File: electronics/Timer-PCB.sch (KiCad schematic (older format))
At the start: 0 parts

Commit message: init first version of PCB
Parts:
- added C1: 120n, Capacitor_THT_k:C_Axial_L5.1mm_D3.1mm_P7.50mm_Horizontal_k, symbol Device_k:C
- added C2: 2200uF, Capacitor_THT_k:CP_Radial_D13.0mm_P5.00mm_k, symbol Device_k:CP
- added C3: 220uF, Capacitor_THT_k:CP_Radial_D8.0mm_P3.50mm_k, symbol Device_k:CP
- added D1: D_Bridge_+-AA, Diode_THT_k:Diode_Bridge_Round_D8.9mm_k, symbol Device_k:D_Bridge_+-AA
- added D2: LED, LED_THT_k:LED_D5.0mm_Clear_k, symbol Device_k:LED
- added J1: Screw_Terminal_01x02, TerminalBlock_Phoenix_k:TerminalBlock_Phoenix_PT-1,5-2-3.5-H_1x02_P3.50mm_Horizontal_k, symbol Connector_k:Screw_Terminal_01x02
- added J2: Screw_Terminal_01x03, TerminalBlock_Phoenix_k:TerminalBlock_Phoenix_PT-1,5-3-3.5-H_1x03_P3.50mm_Horizontal_k, symbol Connector_k:Screw_Terminal_01x03
- added R1: R120, Resistor_THT_k:R_Axial_DIN0207_L6.3mm_D2.5mm_P10.16mm_Horizontal_k, symbol Device_k:R
- added R2: 2k2, Resistor_THT_k:R_Axial_DIN0207_L6.3mm_D2.5mm_P10.16mm_Horizontal_k, symbol Device_k:R
- added SW1: Rotary_Encoder_Switch, Rotary_Encoder_k:RotaryEncoder_Alps_EC11E-Switch_Vertical_H20mm_CircularMountingHoles_k, symbol Device_k:Rotary_Encoder_Switch
- added U1: L7805, Package_TO_SOT_THT_k:TO-220-3_Horizontal_TabDown_k, symbol Regulator_Linear_k:L7805
- added U2: Teensy-LC, Teensy.pretty:Teensy30_31_32_LC, symbol teensy_library:Teensy-LC
- added U3: 7-Seg_8dig_MAX7219, Display_7Segment_k:7seg_8dig_MAX7219_module, symbol Display_Character_k:7-Seg_8dig_MAX7219
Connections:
- net labels added: +5V, CLK, CS, DIN, GND, SSR, VD
- wire segments 0 -> 54
- no-connect marks 0 -> 33
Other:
- note added: "Power Supply"
- note added: "SolidState Relais output"
- note added: "teensy"

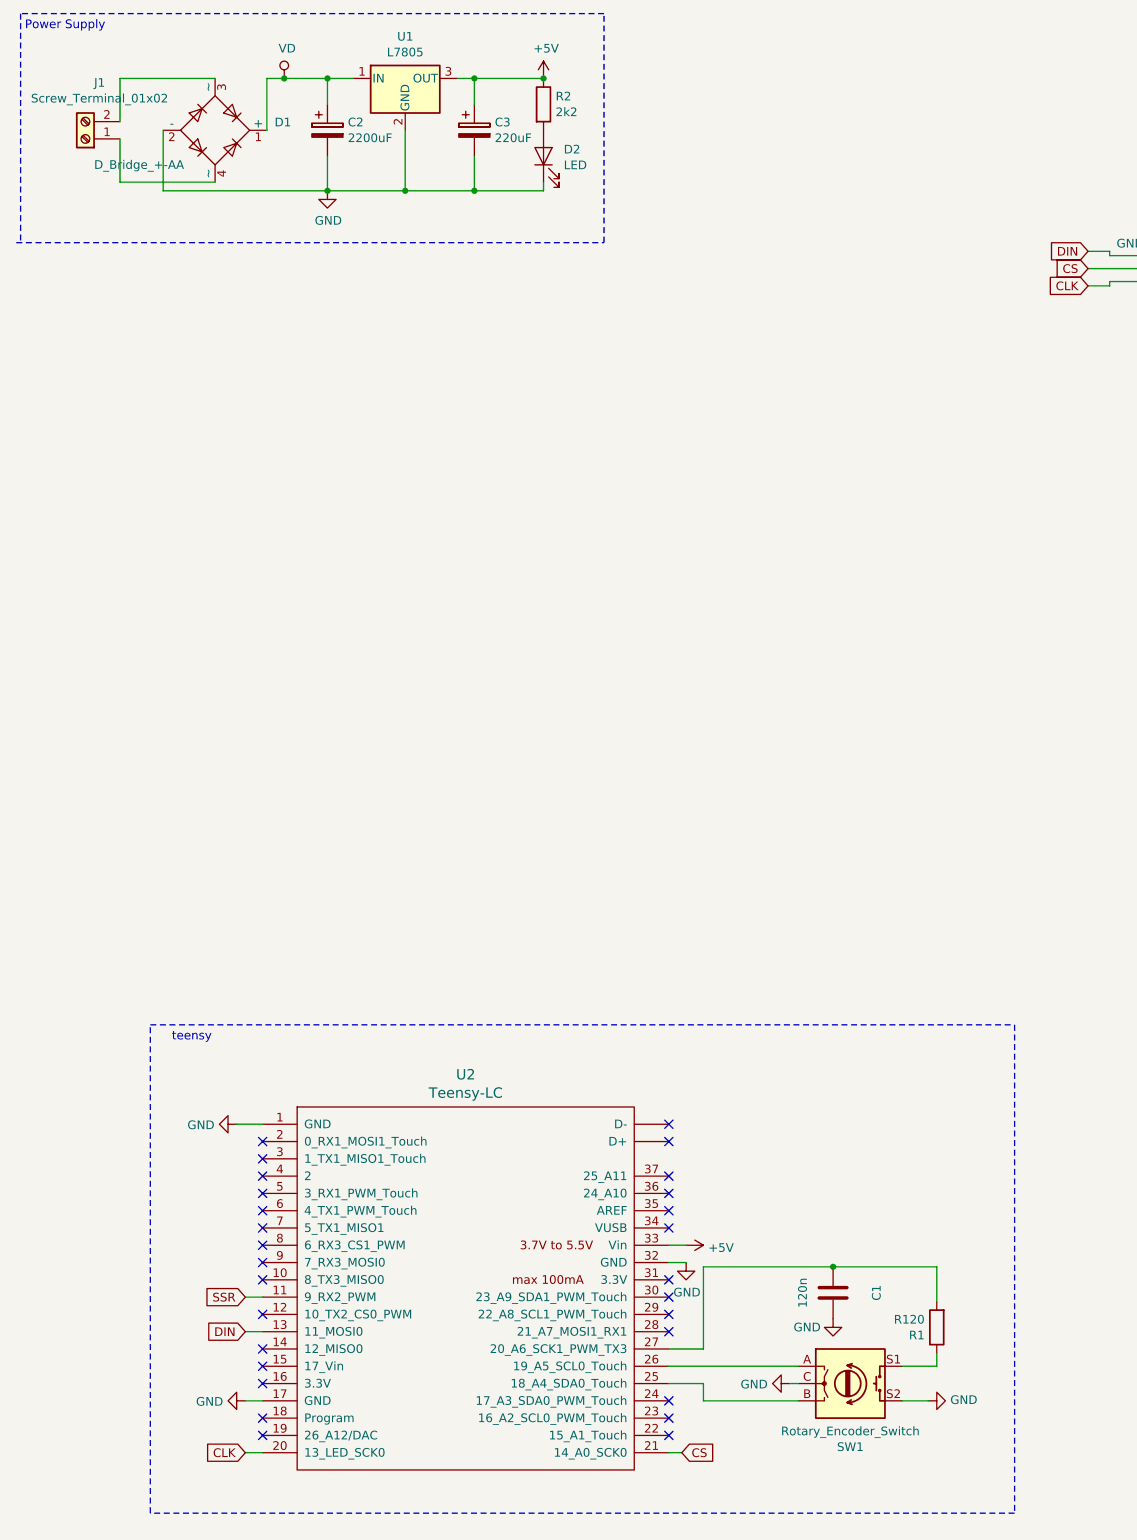
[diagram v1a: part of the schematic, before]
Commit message: changed schematic to use teensy pin for indicator LED (see #3)
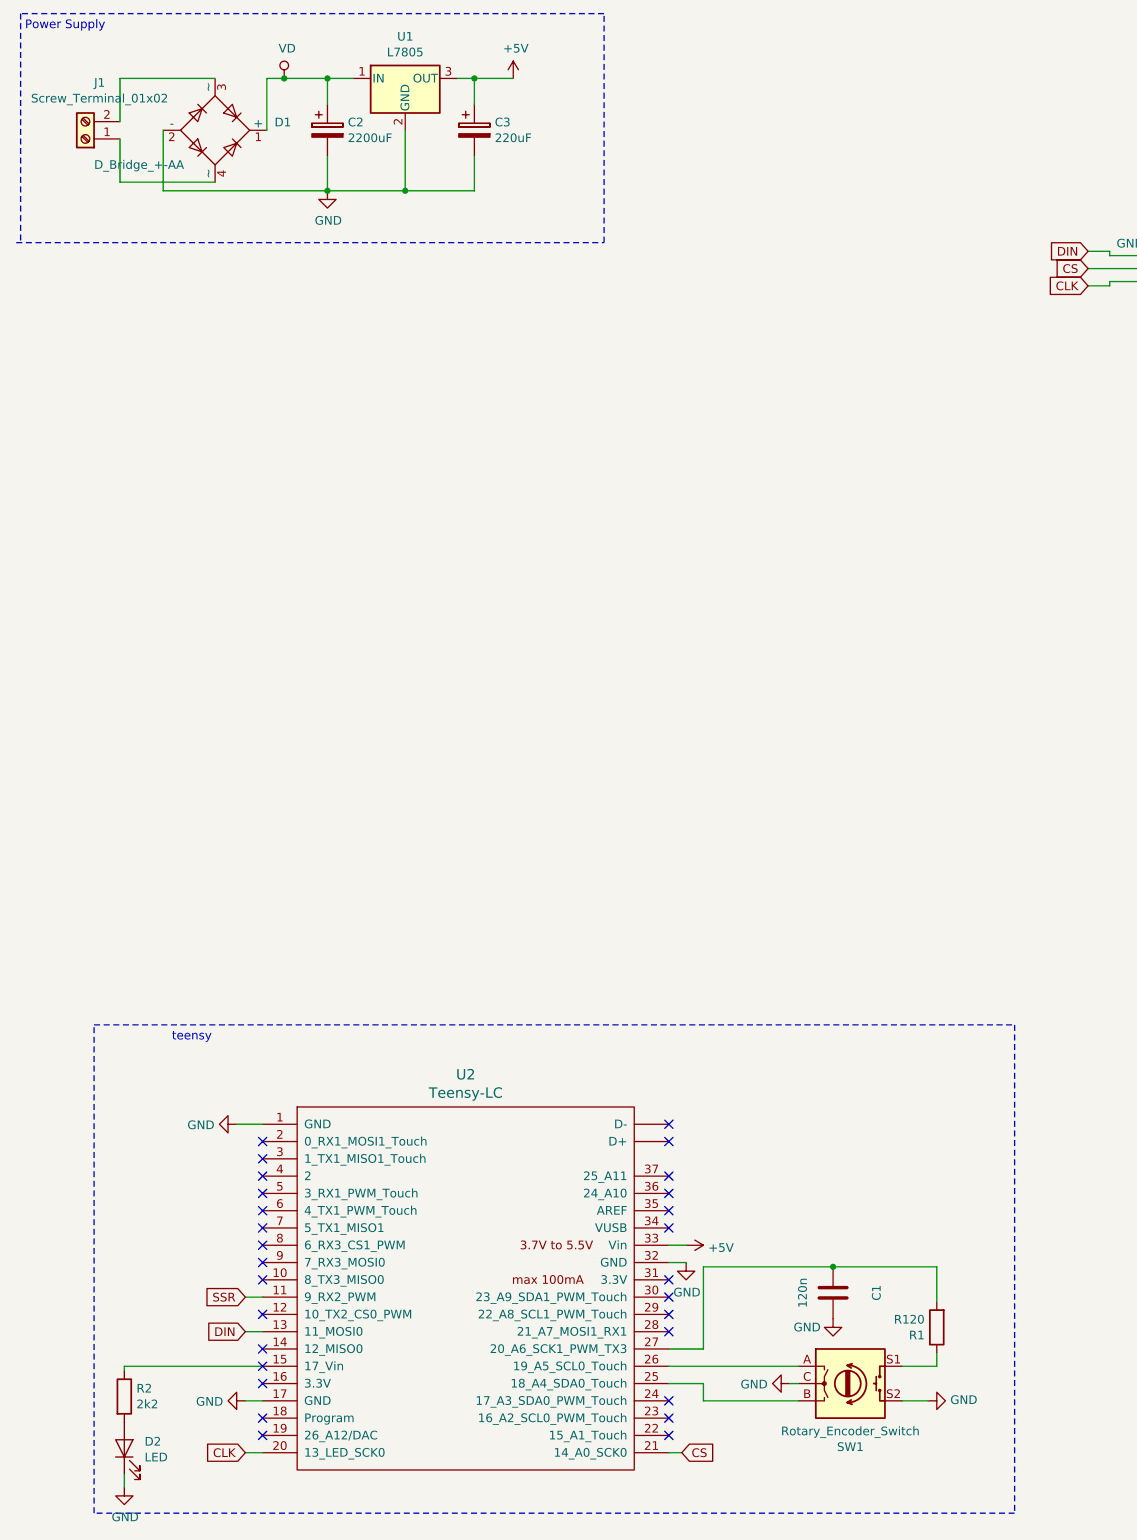
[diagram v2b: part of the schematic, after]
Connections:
- wire segments 54 -> 55
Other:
- moved on the sheet: D2, R2
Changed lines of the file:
@@
 L power_k:+5V #PWR06
 U 1 1 5F7D4ECC
-P 3975 1400
-F 0 "#PWR06" H 3975 1250 50  0001 C CNN
-F 1 "+5V" H 3990 1573 50  0000 C CNN
-F 2 "" H 3975 1400 50  0001 C CNN
-F 3 "" H 3975 1400 50  0001 C CNN
-	1    3975 1400
-	1    0    0    -1
-$EndComp
-Connection ~ 3575 1400
+P 3800 1400
+F 0 "#PWR06" H 3800 1250 50  0001 C CNN
+F 1 "+5V" H 3815 1573 50  0000 C CNN
+F 2 "" H 3800 1400 50  0001 C CNN
+F 3 "" H 3800 1400 50  0001 C CNN
+	1    3800 1400
+	1    0    0    -1
+$EndComp
 $Comp
 L Device_k:R R2
 U 1 1 5F7D5501
-P 3975 1550
-F 0 "R2" H 4045 1596 50  0000 L CNN
-F 1 "2k2" H 4045 1505 50  0000 L CNN
-F 2 "Resistor_THT_k:R_Axial_DIN0207_L6.3mm_D2.5mm_P10.16mm_Horizontal_k" V 3905 1550 50  0001 C CNN
-F 3 "~" H 3975 1550 50  0001 C CNN
-	1    3975 1550
+P 1550 9025
+F 0 "R2" H 1620 9071 50  0000 L CNN
+F 1 "2k2" H 1620 8980 50  0000 L CNN
+F 2 "Resistor_THT_k:R_Axial_DIN0207_L6.3mm_D2.5mm_P10.16mm_Horizontal_k" V 1480 9025 50  0001 C CNN
+F 3 "~" H 1550 9025 50  0001 C CNN
+	1    1550 9025
 	1    0    0    -1
 $EndComp
@@
 L Device_k:LED D2
 U 1 1 5F7D5E21
-P 3975 1850
-F 0 "D2" V 4014 1733 50  0000 R CNN
-F 1 "LED" V 3923 1733 50  0000 R CNN
-F 2 "LED_THT_k:LED_D5.0mm_Clear_k" H 3975 1850 50  0001 C CNN
-F 3 "~" H 3975 1850 50  0001 C CNN
-	1    3975 1850
+P 1550 9325
+F 0 "D2" V 1589 9208 50  0000 R CNN
+F 1 "LED" V 1498 9208 50  0000 R CNN
+F 2 "LED_THT_k:LED_D5.0mm_Clear_k" H 1550 9325 50  0001 C CNN
+F 3 "~" H 1550 9325 50  0001 C CNN
+	1    1550 9325
 	0    -1   -1   0
 $EndComp
-Wire Wire Line
-	3975 2000 3975 2050
 $Comp
 L Device_k:CP C3
@@
 	1    0    0    -1
 $EndComp
-Wire Wire Line
-	3575 1400 3975 1400
-Wire Wire Line
-	3575 2050 3975 2050
-Connection ~ 3575 2050
 $Comp
 L power_k:GND #PWR09
@@
 Text Notes 975  1125 0    50   ~ 0
 Power Supply
-Connection ~ 3975 1400
 Wire Notes Line
 	7875 4750 9900 4750
@@
 NoConn ~ 9725 2575
 Wire Notes Line
-	1700 6875 6700 6875
+	1375 6875 6700 6875
 Wire Notes Line
 	6700 6875 6700 9700
 Wire Notes Line
-	6700 9700 1700 9700
-Wire Notes Line
-	1700 9700 1700 6875
+	6700 9700 1375 9700
+Wire Notes Line
+	1375 9700 1375 6875
 Text Notes 1825 6975 0    50   ~ 0
 teensy
@@
 Wire Wire Line
 	2250 9350 2350 9350
+Wire Wire Line
+	3575 1400 3800 1400
+Connection ~ 3575 1400
+Wire Wire Line
+	2350 8850 1550 8850
+Wire Wire Line
+	1550 8850 1550 8875
+$Comp
+L power_k:GND #PWR?
+U 1 1 5FF58D4F
+P 1550 9550
+F 0 "#PWR?" H 1550 9300 50  0001 C CNN
+F 1 "GND" H 1555 9377 50  0000 C CNN
+F 2 "" H 1550 9550 50  0001 C CNN
+F 3 "" H 1550 9550 50  0001 C CNN
+	1    1550 9550
+	1    0    0    -1
+$EndComp
+Wire Wire Line
+	1550 9550 1550 9475
 $EndSCHEMATC

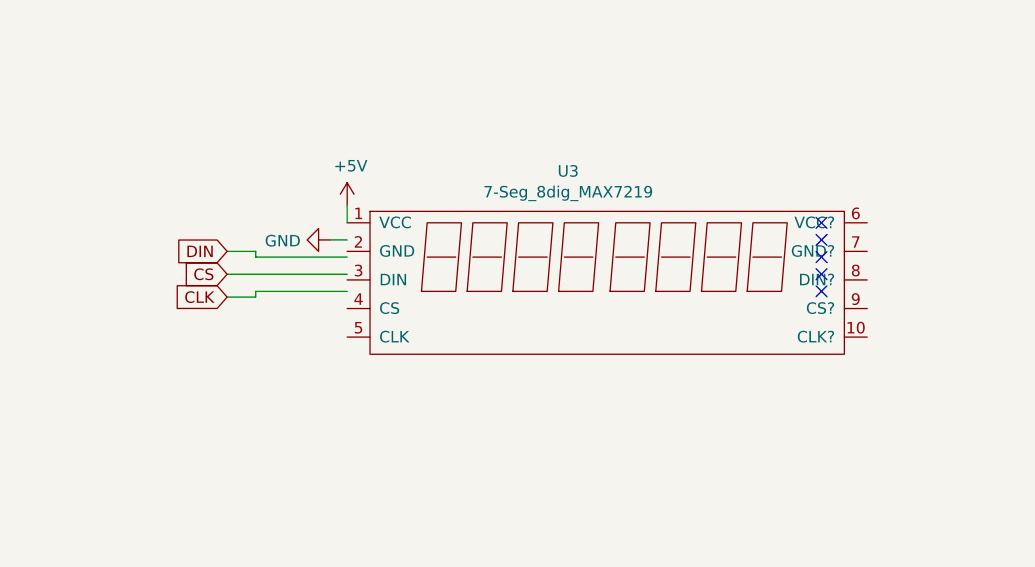
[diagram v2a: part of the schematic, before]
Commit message: changed symbol for display
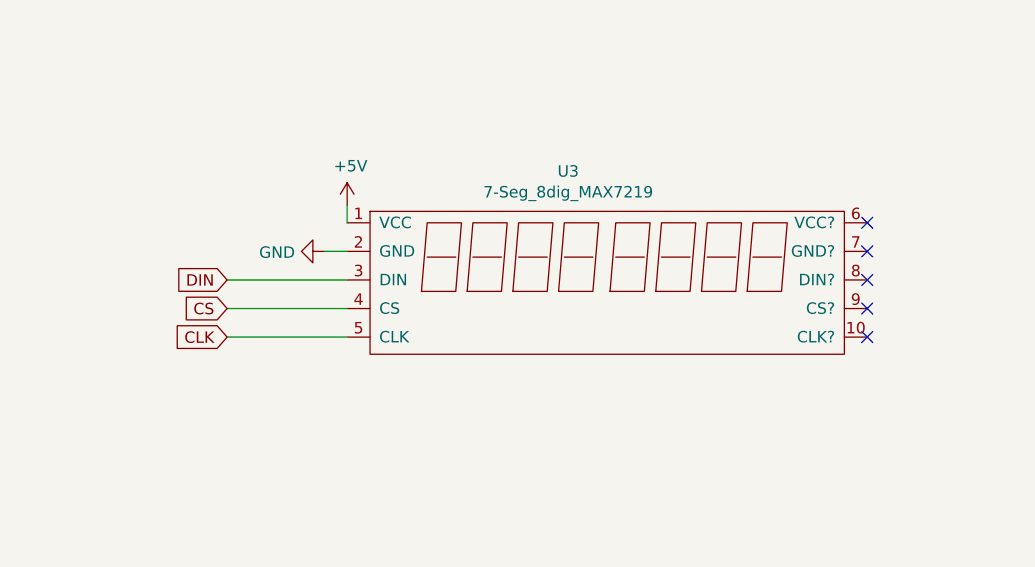
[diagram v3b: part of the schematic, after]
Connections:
- wire segments 55 -> 51
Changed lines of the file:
@@
 L power_k:GND #PWR09
 U 1 1 5F7D9FF0
-P 7575 2350
-F 0 "#PWR09" H 7575 2100 50  0001 C CNN
-F 1 "GND" V 7580 2222 50  0000 R CNN
-F 2 "" H 7575 2350 50  0001 C CNN
-F 3 "" H 7575 2350 50  0001 C CNN
-	1    7575 2350
-	0    1    1    0
-$EndComp
-Wire Wire Line
-	7575 2350 7650 2350
+P 7550 2400
+F 0 "#PWR09" H 7550 2150 50  0001 C CNN
+F 1 "GND" V 7555 2272 50  0000 R CNN
+F 2 "" H 7550 2400 50  0001 C CNN
+F 3 "" H 7550 2400 50  0001 C CNN
+	1    7550 2400
+	0    1    1    0
+$EndComp
+Wire Wire Line
+	7550 2400 7650 2400
 $Comp
 L power_k:+5V #PWR010
@@
 Wire Wire Line
 	7650 2200 7650 2275
-Text GLabel 7125 2400 0    50   Input ~ 0
+Text GLabel 7125 2525 0    50   Input ~ 0
 DIN
-Wire Wire Line
-	7125 2400 7250 2400
-Wire Wire Line
-	7250 2400 7250 2425
-Wire Wire Line
-	7250 2425 7650 2425
-Text GLabel 7125 2500 0    50   Input ~ 0
+Text GLabel 7125 2650 0    50   Input ~ 0
 CS
-Text GLabel 7125 2600 0    50   Input ~ 0
+Text GLabel 7125 2775 0    50   Input ~ 0
 CLK
-Wire Wire Line
-	7125 2500 7650 2500
-Wire Wire Line
-	7125 2600 7250 2600
-Wire Wire Line
-	7250 2600 7250 2575
-Wire Wire Line
-	7250 2575 7650 2575
 Text GLabel 2250 9350 0    50   Input ~ 0
 CLK
@@
 NoConn ~ 4700 9250
 NoConn ~ 2350 8850
-NoConn ~ 9725 2275
-NoConn ~ 9725 2350
-NoConn ~ 9725 2425
-NoConn ~ 9725 2500
-NoConn ~ 9725 2575
+NoConn ~ 9925 2400
+NoConn ~ 9925 2525
+NoConn ~ 9925 2650
 Wire Notes Line
 	1375 6875 6700 6875
@@
 Wire Wire Line
 	1550 9550 1550 9475
+Wire Wire Line
+	7125 2775 7650 2775
+Wire Wire Line
+	7650 2525 7125 2525
+Wire Wire Line
+	7650 2650 7125 2650
+NoConn ~ 9925 2275
+NoConn ~ 9925 2775
 $EndSCHEMATC
